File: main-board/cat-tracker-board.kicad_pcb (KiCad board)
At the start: 2 copper layers, 51.7 x 23.1 mm, 31 parts, among them J1 Conn_01x10, J3 USB_B_Micro, Q1 SI3443DDV-T1-GE3, SW1 PCM12SMTR, U1 ATSAMD21E18A-M, U3 L80-R, U4 RFM95W-915S2, U5 MCP73831-2ACI/MC, U6 MCP1700T-3602E/TT

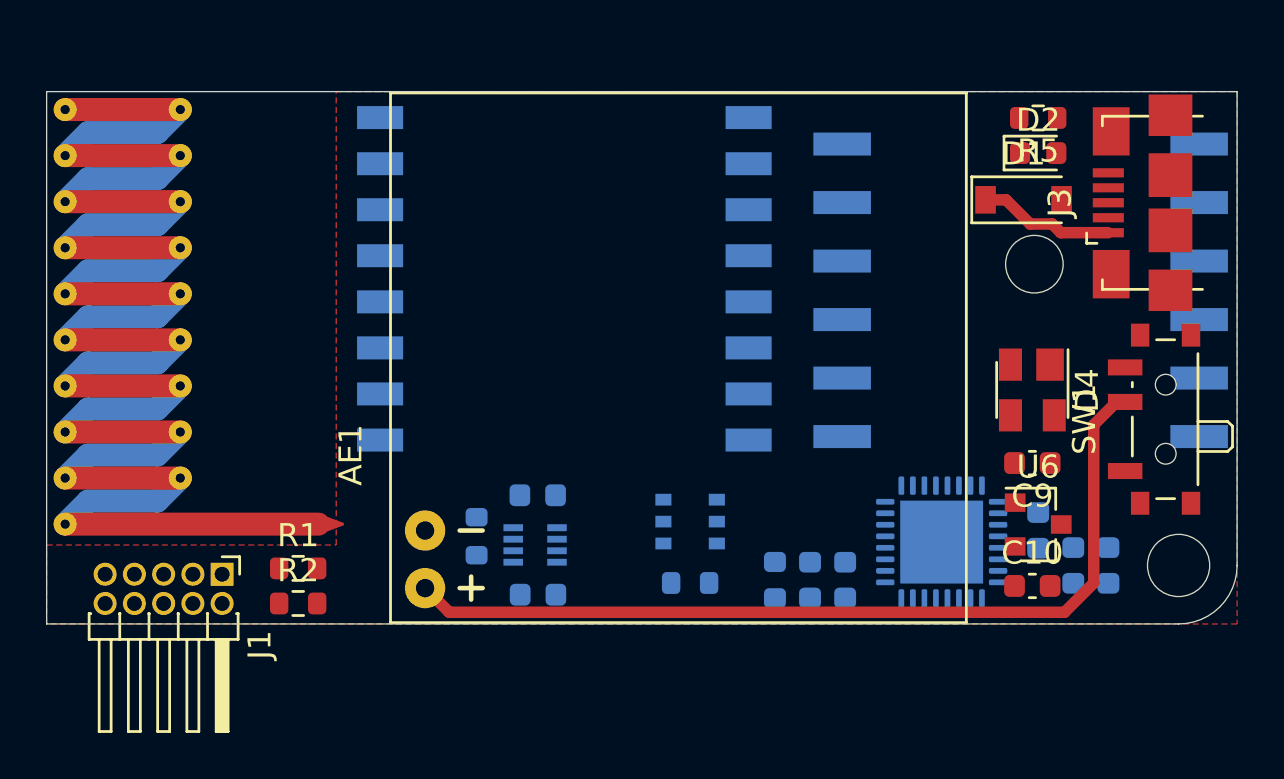
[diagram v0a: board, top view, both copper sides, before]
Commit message: Add some tracks.
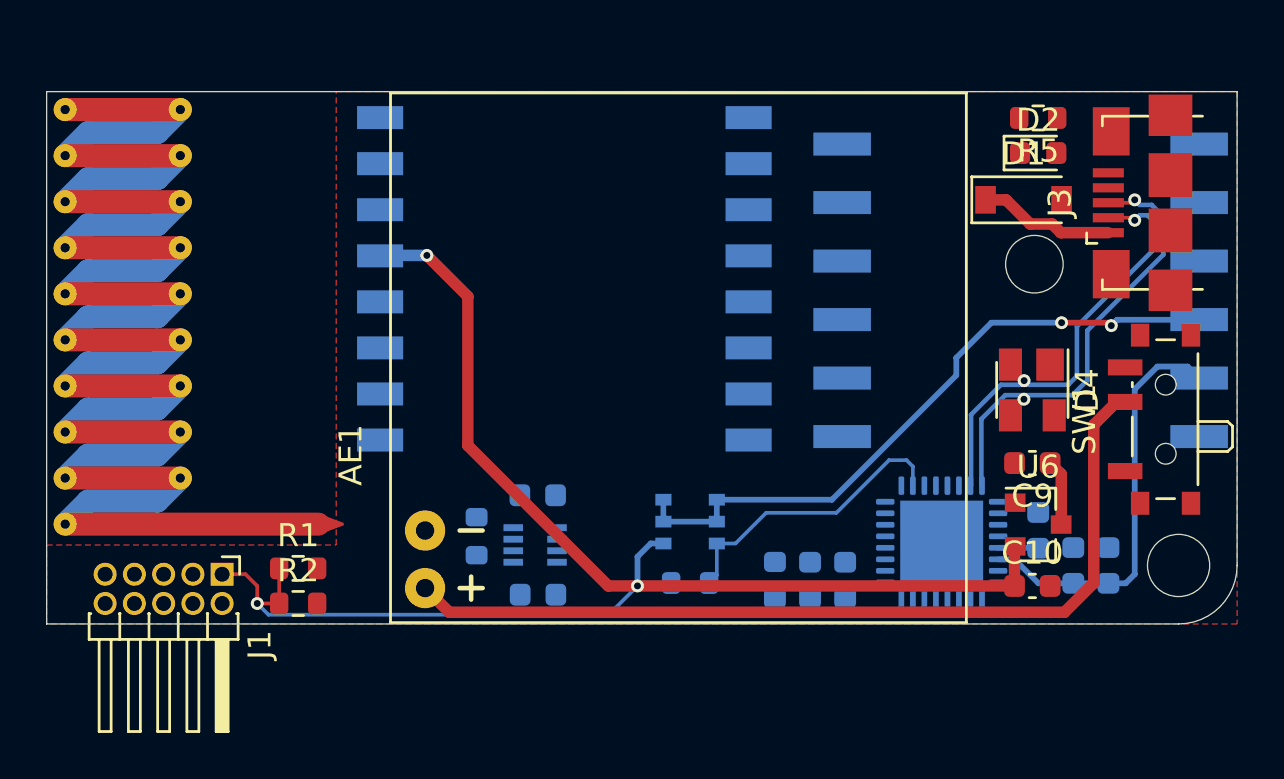
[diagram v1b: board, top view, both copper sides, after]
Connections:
- J1 pad 1: (no net) -> /VDD
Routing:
- net /VDD: track 0.00 -> 83.3 mm, vias 0 -> 3
- net Net-(Q1-Pad1): track 0.00 -> 29.0 mm, vias 0 -> 2
- net /USBD+: track 0.00 -> 20.4 mm, vias 0 -> 2
- net /USBD-: track 0.00 -> 19.6 mm, vias 0 -> 2
- net /GPS_EN: track 0.00 -> 12.8 mm
- net Net-(C9-Pad1): track 0.00 -> 2.87 mm
- net Net-(C1-Pad2): track 0.00 -> 1.75 mm

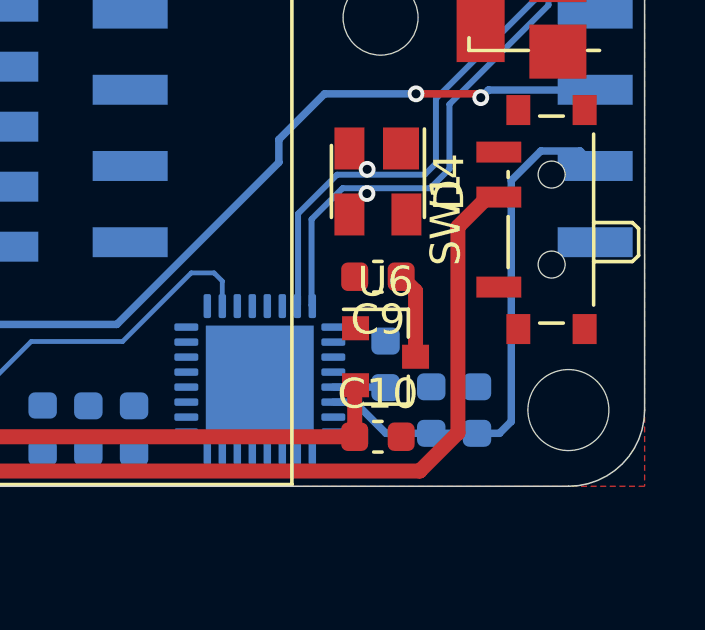
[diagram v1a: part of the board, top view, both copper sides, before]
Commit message: Change switch connection to improve layout.
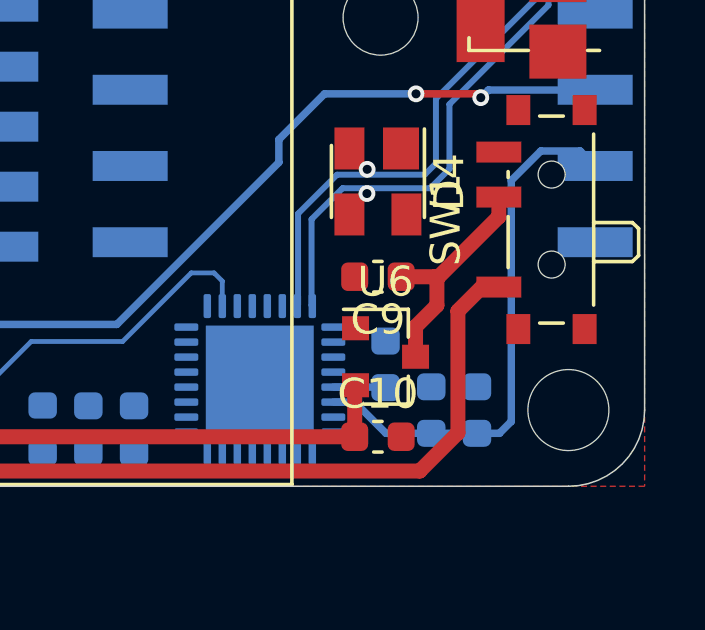
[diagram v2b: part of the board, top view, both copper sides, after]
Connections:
- SW1 pad 1: (no net) -> /VBAT
- SW1 pad 2: /VBAT -> Net-(C9-Pad1)
- SW1 pad 3: Net-(C9-Pad1) -> (no net)
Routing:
- net Net-(C9-Pad1): track 2.87 -> 8.06 mm
- net /VBAT: track 38.6 -> 35.8 mm

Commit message: Work on layout.
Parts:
- moved R1 0.25 mm to (10.9, 20.4)
- moved R2 0.25 mm to (10.9, 22.0)
- moved J1 0.25 mm to (7.62, 20.7)
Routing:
- net /nRESET: track 0.00 -> 49.4 mm, vias 0 -> 3
- net /VUSB: track 5.92 -> 47.5 mm, vias 0 -> 2
- net Net-(D2-Pad1): track 0.00 -> 39.0 mm, vias 0 -> 1
- net /GND: track 0.00 -> 16.2 mm, vias 0 -> 5
- net /SWCLK: track 0.00 -> 9.92 mm
- net Net-(C4-Pad1): track 0.00 -> 5.08 mm
- net /VBAT: track 35.8 -> 38.3 mm
- net Net-(D2-Pad2): track 0.00 -> 1.54 mm

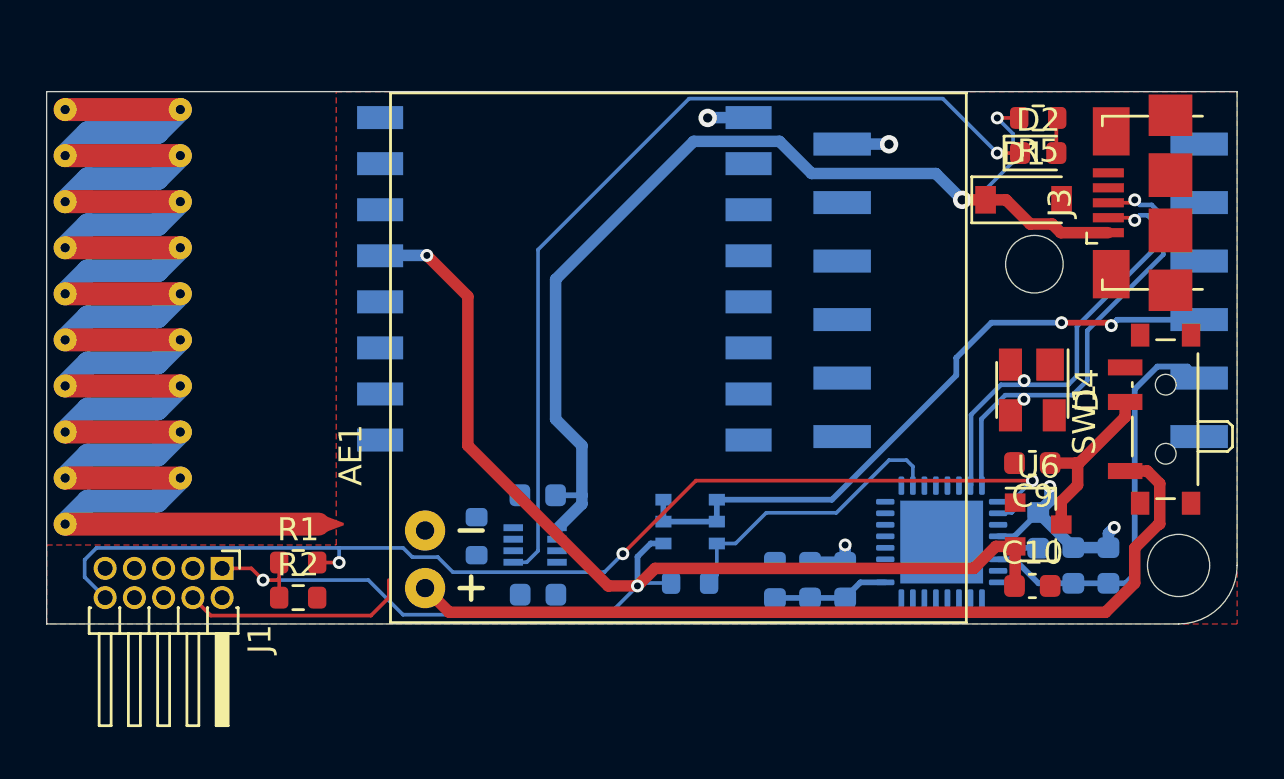
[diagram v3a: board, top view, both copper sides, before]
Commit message: Correct footprint assignment for U5 and work on layout.
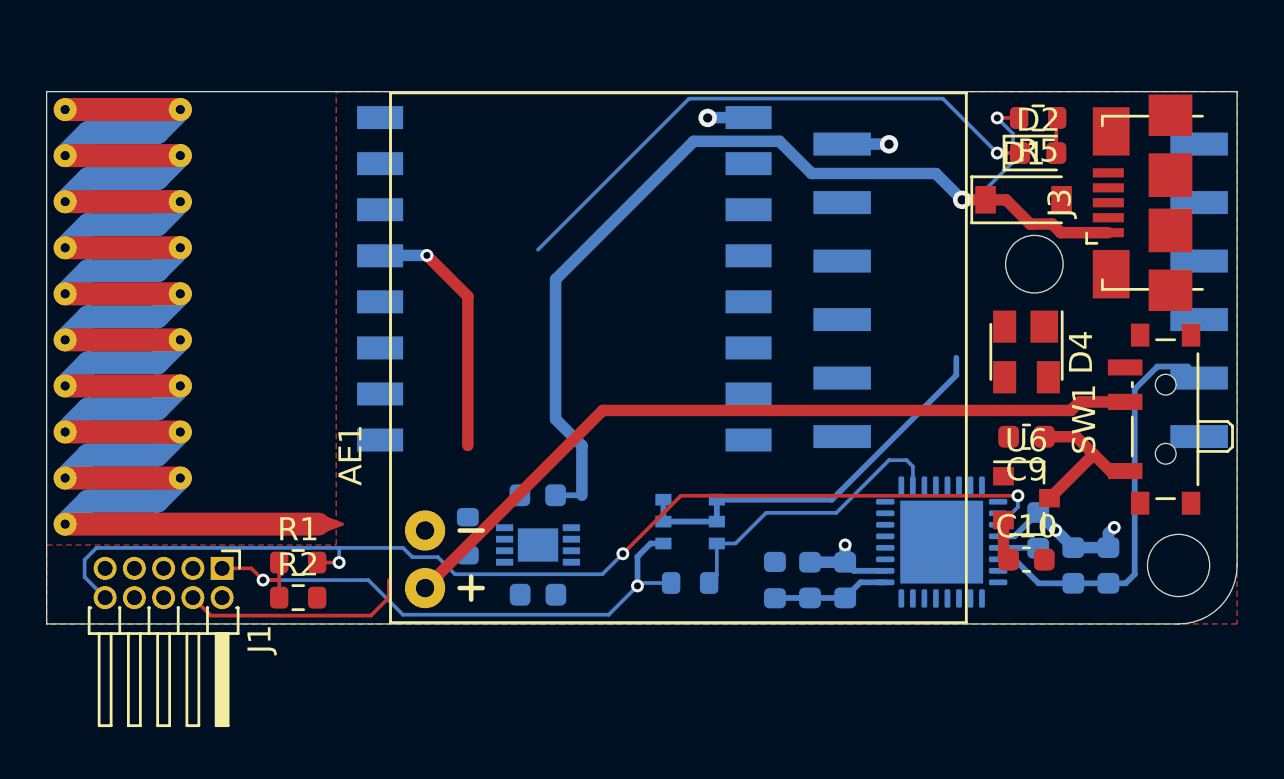
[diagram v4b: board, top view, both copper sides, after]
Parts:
- U5: footprint Package_DFN_QFN:DFN-8_2x2mm_P0.5mm -> Package_DFN_QFN:DFN-8-1EP_3x2mm_P0.5mm_EP1.75x1.45mm
- moved D4 1.67 mm to (42.5, 11.3)
- moved U6 1.25 mm to (42.5, 17.7)
- moved C10 1.17 mm to (42.5, 20.3)
- moved C9 1.17 mm to (42.5, 15.0)
- moved R6 0.38 mm to (18.3, 19.3)
- moved U5 0.13 mm to (21.3, 19.7)
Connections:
- SW1 pad 1: /VBAT -> Net-(C9-Pad1)
- SW1 pad 2: Net-(C9-Pad1) -> /VBAT
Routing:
- net /VDD: track 83.6 -> 56.6 mm
- net /USBD+: track 20.4 -> 0.00 mm, vias 2 -> 0
- net /USBD-: track 19.6 -> 0.00 mm, vias 2 -> 0
- net Net-(D2-Pad1): track 39.0 -> 24.6 mm
- net Net-(Q1-Pad1): track 29.0 -> 17.6 mm, vias 2 -> 0
- net /VBAT: track 38.3 -> 34.1 mm
- net /VUSB: track 47.5 -> 45.2 mm
- net /nRESET: track 49.4 -> 47.7 mm
- net /GND: track 16.2 -> 14.8 mm
- net Net-(C9-Pad1): track 8.06 -> 6.84 mm

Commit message: Work on layout.
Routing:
- net /SWDIO: track 0.00 -> 39.0 mm, vias 0 -> 4
- net /SWCLK: track 9.92 -> 39.0 mm, vias 0 -> 1
- net /VDD: track 56.6 -> 84.3 mm, vias 3 -> 6
- net Net-(D2-Pad1): track 24.6 -> 46.0 mm, vias 1 -> 3
- net /GND: track 14.8 -> 28.3 mm, vias 5 -> 6
- net /VBAT: track 34.1 -> 37.9 mm, vias 0 -> 1
- net Net-(R6-Pad1): track 0.00 -> 1.79 mm
- net /VUSB: track 45.2 -> 46.4 mm
- net /nRESET: track 47.7 -> 48.3 mm, vias 3 -> 5

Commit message: Route almost everything.
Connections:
- U1 pad 33: (no net) -> /GND
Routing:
- net /RFM_INT: track 0.00 -> 30.7 mm, vias 0 -> 4
- net /GND: track 28.3 -> 55.3 mm, vias 6 -> 15
- net /GPS_TX: track 0.00 -> 23.8 mm, vias 0 -> 2
- net /MOSI: track 0.00 -> 23.3 mm, vias 0 -> 2
- net /GPS_RX: track 0.00 -> 23.3 mm, vias 0 -> 2
- net /USBD-: track 0.00 -> 21.6 mm, vias 0 -> 2
- net /MISO: track 0.00 -> 20.7 mm, vias 0 -> 2
- net /SCK: track 0.00 -> 20.3 mm, vias 0 -> 2
- net /USBD+: track 0.00 -> 19.6 mm, vias 0 -> 2
- net /NSS: track 0.00 -> 15.3 mm, vias 0 -> 2
- net Net-(Q1-Pad1): track 17.6 -> 32.7 mm, vias 0 -> 2
- net /GPS_nRESET: track 0.00 -> 14.5 mm, vias 0 -> 4
- net /GPS_1PPS: track 0.00 -> 12.3 mm, vias 0 -> 4
- net /RFM_RESET: track 0.00 -> 11.7 mm, vias 0 -> 2
- net /VUSB: track 46.4 -> 53.3 mm
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
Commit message: Update to KiCad v6
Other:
- net class Default removed

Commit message: Add antenna matching, update some PNs
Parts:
- added C8: 1 pF, Capacitor_SMD:C_0603_1608Metric, F.Cu at (14.2, 16.6)
- added L1: 12 nH, Inductor_SMD:L_0603_1608Metric, F.Cu at (13.0, 18.0)
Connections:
- J1 pad 6: (no net) -> unconnected-(J1-Pad6)
- J1 pad 7: (no net) -> unconnected-(J1-Pad7)
- J1 pad 8: (no net) -> unconnected-(J1-Pad8)
- J1 pad 9: (no net) -> unconnected-(J1-Pad9)
- J3 pad 4: (no net) -> unconnected-(J3-Pad4)
- SW1 pad 3: (no net) -> unconnected-(SW1-Pad3)
- U1 pad 1: (no net) -> unconnected-(U1-Pad1)
- U1 pad 2: (no net) -> unconnected-(U1-Pad2)
- U1 pad 22: (no net) -> unconnected-(U1-Pad22)
- U1 pad 25: (no net) -> unconnected-(U1-Pad25)
- U1 pad 27: (no net) -> unconnected-(U1-Pad27)
- U1 pad 3: (no net) -> unconnected-(U1-Pad3)
- U1 pad 4: (no net) -> unconnected-(U1-Pad4)
- U1 pad 5: (no net) -> unconnected-(U1-Pad5)
- U1 pad 6: (no net) -> unconnected-(U1-Pad6)
- U1 pad 7: (no net) -> unconnected-(U1-Pad7)
- U1 pad 8: (no net) -> unconnected-(U1-Pad8)
- U3 pad 11: (no net) -> unconnected-(U3-Pad11)
- U3 pad 7: (no net) -> unconnected-(U3-Pad7)
- U3 pad 8: (no net) -> unconnected-(U3-Pad8)
- U3 pad 9: (no net) -> unconnected-(U3-Pad9)
- U4 pad 11: (no net) -> unconnected-(U4-Pad11)
- U4 pad 12: (no net) -> unconnected-(U4-Pad12)
- U4 pad 15: (no net) -> unconnected-(U4-Pad15)
- U4 pad 16: (no net) -> unconnected-(U4-Pad16)
- U4 pad 7: (no net) -> unconnected-(U4-Pad7)
- U4 pad 9: Net-(AE1-Pad1) -> Net-(U4-Pad9)
- U5 pad 7: (no net) -> unconnected-(U5-Pad7)
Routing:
- net Net-(AE1-Pad1): track 0.00 -> 2.51 mm
- net Net-(D2-Pad1): track 46.4 -> 47.8 mm
- net Net-(U4-Pad9): track 0.00 -> 1.02 mm, vias 0 -> 1
